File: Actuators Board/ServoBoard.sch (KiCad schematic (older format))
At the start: 56 parts, among them J10 Conn_01x02_Male, J9 Conn_01x02_Male, Q1 MMDT2222A

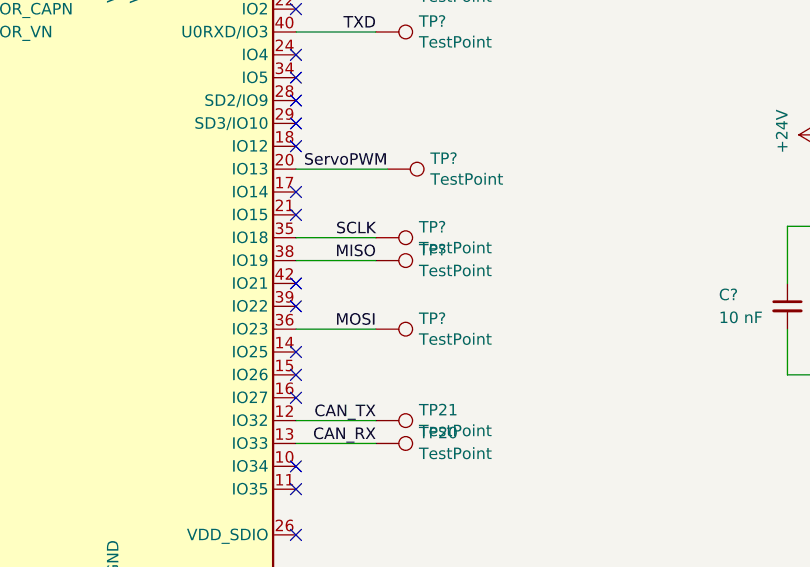
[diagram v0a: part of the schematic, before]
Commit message: servo sclk, miso and mosi pins removed
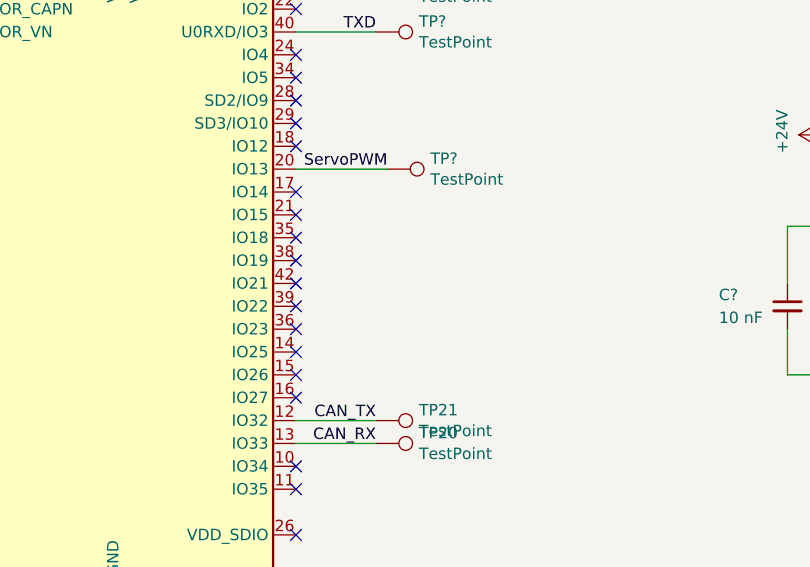
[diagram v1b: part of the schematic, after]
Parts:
- removed TP? (x3): TestPoint, symbol Connector:TestPoint
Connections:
- net MISO: no longer names the net of U?.38 (IO19)
- net MOSI: no longer names the net of U?.36 (IO23)
- net SCLK: no longer names the net of U?.35 (IO18)
- no-connect marks 30 -> 33
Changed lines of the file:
@@
 Text Notes 10600 7700 0    50   ~ 0
 0.1\n\n
-Text Label 5350 3650 2    50   ~ 0
-MISO
-Text Label 5350 3550 2    50   ~ 0
-SCLK
 Text Label 1550 7550 2    50   ~ 0
 EN
@@
 Wire Wire Line
 	5000 2650 5350 2650
-Wire Wire Line
-	5000 3550 5350 3550
-Wire Wire Line
-	5000 3650 5350 3650
-Wire Wire Line
-	5000 3950 5350 3950
 Text Label 5350 2450 2    50   ~ 0
 RXD
@@
 Text Label 5350 4350 2    50   ~ 0
 CAN_TX
-Text Label 5350 3950 2    50   ~ 0
-MOSI
 Wire Wire Line
 	2300 850  2300 1600
@@
 $Comp
 L Connector:TestPoint TP?
-U 1 1 61AFEC97
-P 5350 3950
-F 0 "TP?" V 5304 4138 50  0000 L CNN
-F 1 "TestPoint" V 5395 4138 50  0000 L CNN
-F 2 "" H 5550 3950 50  0001 C CNN
-F 3 "~" H 5550 3950 50  0001 C CNN
-	1    5350 3950
-	0    1    1    0
-$EndComp
-$Comp
-L Connector:TestPoint TP?
-U 1 1 61AFFB17
-P 5350 3650
-F 0 "TP?" V 5304 3838 50  0000 L CNN
-F 1 "TestPoint" V 5395 3838 50  0000 L CNN
-F 2 "" H 5550 3650 50  0001 C CNN
-F 3 "~" H 5550 3650 50  0001 C CNN
-	1    5350 3650
-	0    1    1    0
-$EndComp
-$Comp
-L Connector:TestPoint TP?
-U 1 1 61B06C77
-P 5350 3550
-F 0 "TP?" V 5304 3738 50  0000 L CNN
-F 1 "TestPoint" V 5395 3738 50  0000 L CNN
-F 2 "" H 5550 3550 50  0001 C CNN
-F 3 "~" H 5550 3550 50  0001 C CNN
-	1    5350 3550
-	0    1    1    0
-$EndComp
-$Comp
-L Connector:TestPoint TP?
 U 1 1 61B0E262
 P 5400 3250
@@
 Text Label 9150 2150 0    50   ~ 0
 CAN_LOW
+NoConn ~ 5000 3550
+NoConn ~ 5000 3650
+NoConn ~ 5000 3950
 $EndSCHEMATC

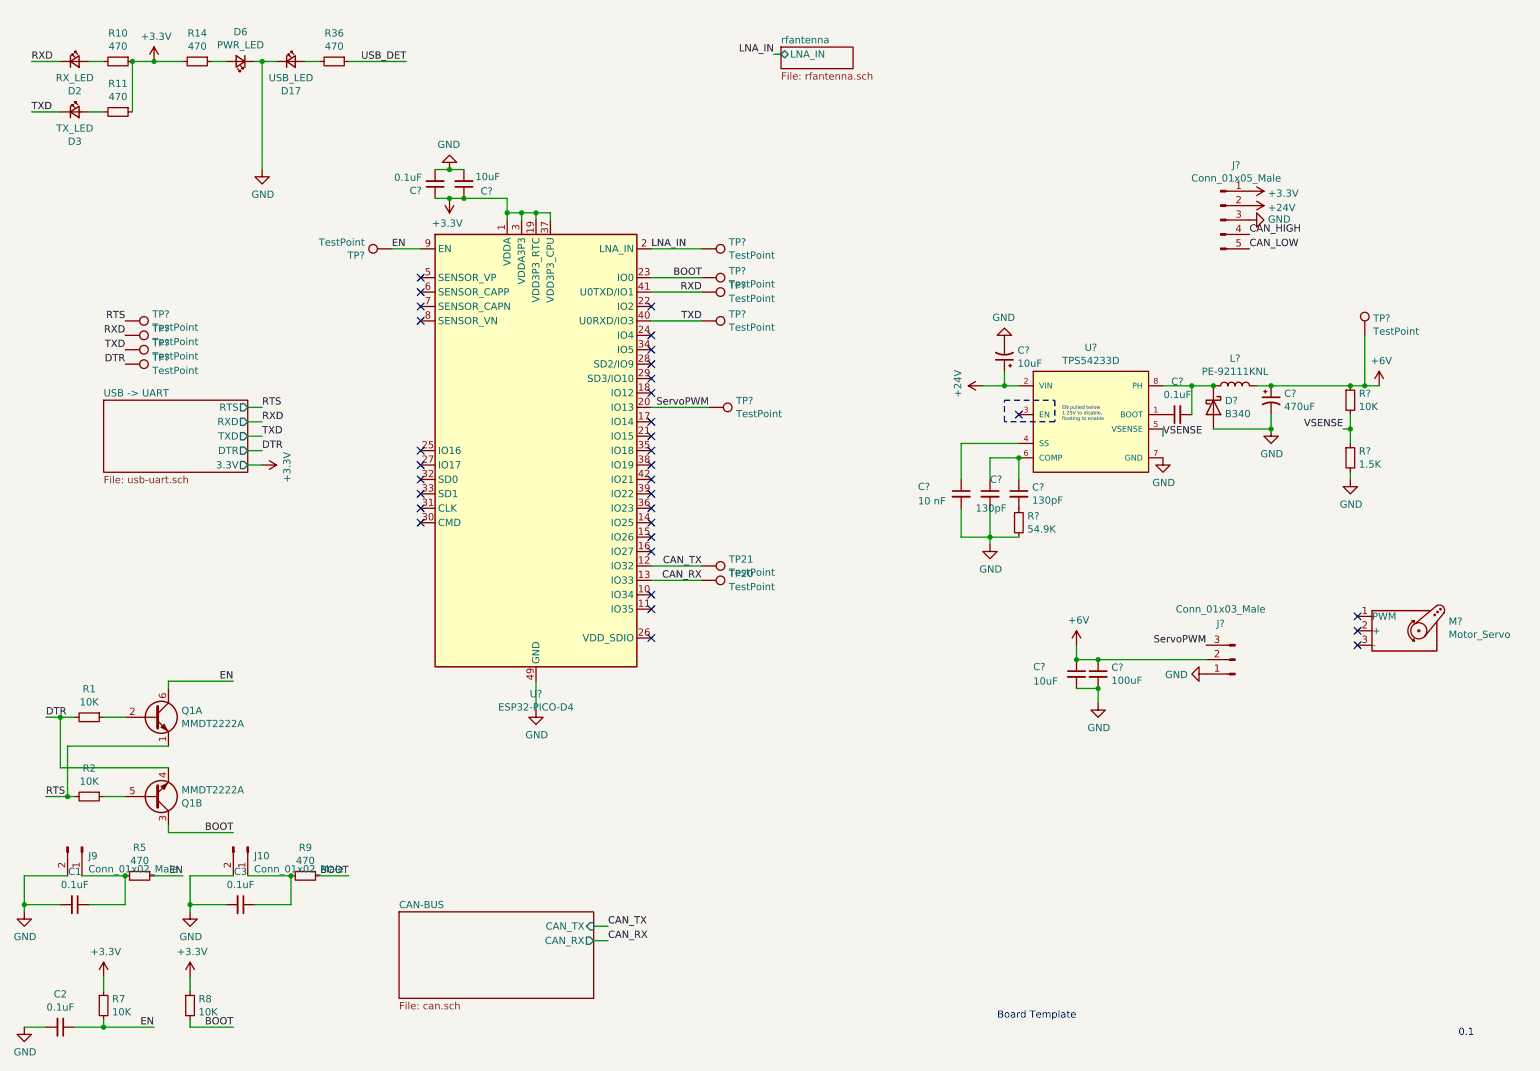
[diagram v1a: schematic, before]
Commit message: 24V LED and CAN pins added (plus tp)
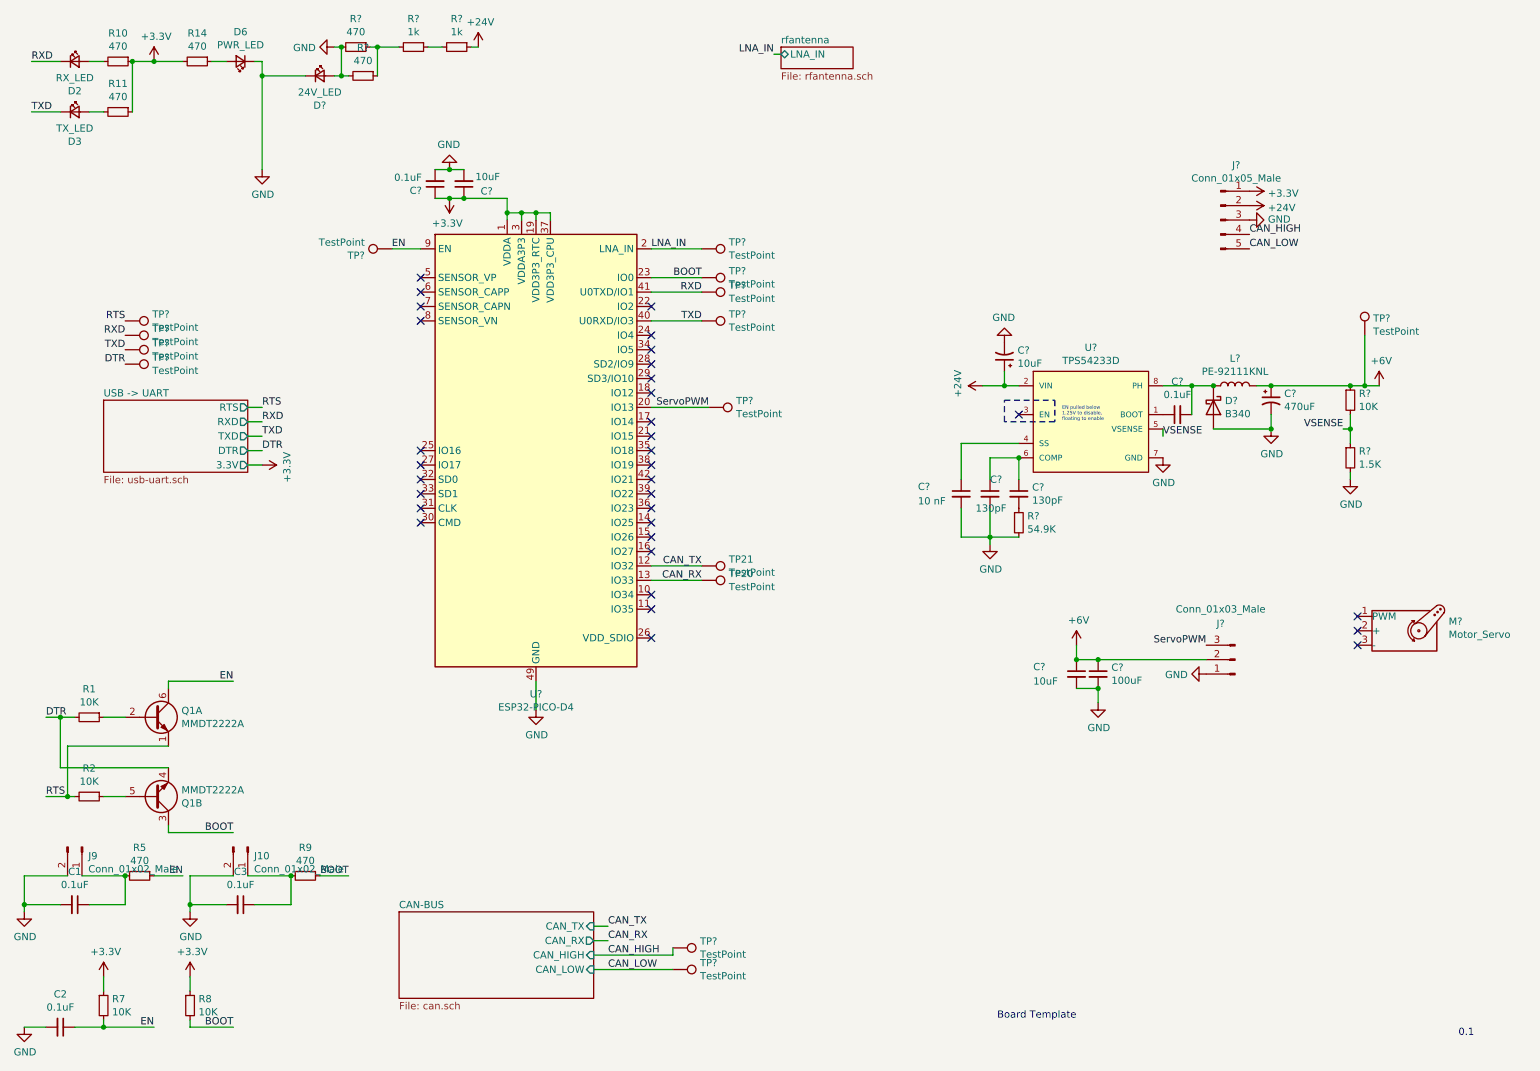
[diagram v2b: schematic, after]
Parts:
- removed D17: USB_LED, LED_SMD:LED_0603_1608Metric_Castellated, symbol Device:LED_Small
- removed R36: 470, Resistor_SMD:R_0603_1608Metric, symbol Device:R_Small
- added D?: 24V_LED, LED_SMD:LED_0603_1608Metric_Castellated, symbol Device:LED_Small
- added R? (x2): 470, Resistor_SMD:R_0603_1608Metric, symbol Device:R_Small
- added R? (x2): 1k, Resistor_SMD:R_0603_1608Metric, symbol Device:R_Small
- added TP? (x2): TestPoint, symbol Connector:TestPoint
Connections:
- net +24V: now also R?.1
- net CAN_HIGH: now also TP?.1
- net CAN_LOW: now also TP?.1
- net GND: now also D?.1 (K), D?.2 (A), R?.2, R?.2
- new net: R?.1, R?.1, R?.2
- new net: R?.1, R?.2

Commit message: Changed sheet title in title card for all boards
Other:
- note added: "Servo Control Board"
- note removed: "Board Template\n"
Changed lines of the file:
@@
 	1    0    0    1
 $EndComp
-Text Notes 7400 7500 0    50   ~ 0
-Board Template\n
+Text Notes 7350 7500 0    50   ~ 0
+Servo Control Board
 $Sheet
 S 1200 3200 1000 500

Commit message: Assigned footprints, changed sense resistor value, added diode to UART
Sense resistor on the buck converter changed from 1.5K to 1.54K to more closely match 6V. Also added a diode on the 3.3V output on the USB-UART converter.
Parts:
- R?: value 1.5K -> 1.54K
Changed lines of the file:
@@
 P 9850 3600
 F 0 "R?" H 9909 3646 50  0000 L CNN
-F 1 "1.5K" H 9909 3555 50  0000 L CNN
+F 1 "1.54K" H 9909 3555 50  0000 L CNN
 F 2 "" H 9850 3600 50  0001 C CNN
 F 3 "~" H 9850 3600 50  0001 C CNN
